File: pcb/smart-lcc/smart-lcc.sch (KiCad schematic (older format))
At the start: 12 parts, among them J1 Control board connector, J2 Aux connector, J3 Conn_01x24 (mirrored), SW1 SW_Push, SW2 SW_Push, U1 ABX00027

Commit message: WIP
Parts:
- removed J1: Control board connector, Connector_PinHeader_2.54mm:PinHeader_1x06_P2.54mm_Vertical, symbol Connector:Conn_01x06_Male
- added J1: 280372-1, TE_280372-1, symbol TE_280372-1:280372-1
- C3: footprint Capacitor_SMD:C_0603_1608Metric -> Capacitor_SMD:C_1206_3216Metric
- R1, R2: footprint Resistor_SMD:R_0402_1005Metric -> Resistor_SMD:R_0603_1608Metric
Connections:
- net +12V: now also J1.1
- net 3V3_MCU: now also J1.6
- net 3V3_OLED: now also J1.5
- net GND: now also J1.4
- net RX_FROM_CONTROL_BOARD_5V: now also J1.3
- net TX_TO_CONTROL_BOARD: now also J1.2
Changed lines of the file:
@@
 F 0 "R2" V 1243 3700 50  0000 C CNN
 F 1 "3K3" V 1334 3700 50  0000 C CNN
-F 2 "Resistor_SMD:R_0402_1005Metric" V 1380 3700 50  0001 C CNN
+F 2 "Resistor_SMD:R_0603_1608Metric" V 1380 3700 50  0001 C CNN
 F 3 "~" H 1450 3700 50  0001 C CNN
 	1    1450 3700
@@
 F 0 "R1" V 943 3700 50  0000 C CNN
 F 1 "2K2" V 1034 3700 50  0000 C CNN
-F 2 "Resistor_SMD:R_0402_1005Metric" V 1080 3700 50  0001 C CNN
+F 2 "Resistor_SMD:R_0603_1608Metric" V 1080 3700 50  0001 C CNN
 F 3 "~" H 1150 3700 50  0001 C CNN
 	1    1150 3700
 	0    1    1    0
 $EndComp
-Text GLabel 1050 1050 2    50   Output ~ 0
+Text GLabel 1750 950  0    50   Output ~ 0
 RX_FROM_CONTROL_BOARD_5V
-Text GLabel 1050 950  2    50   Input ~ 0
+Text GLabel 1750 850  0    50   Input ~ 0
 TX_TO_CONTROL_BOARD
 $Comp
@@
 Text GLabel 1050 2150 2    50   UnSpc ~ 0
 3V3_OLED
-Text GLabel 1050 1250 2    50   UnSpc ~ 0
+Text GLabel 1750 1150 0    50   UnSpc ~ 0
 3V3_OLED
 $Comp
@@
 L power:+12V #PWR0103
 U 1 1 60D7DDC1
-P 1050 850
-F 0 "#PWR0103" H 1050 700 50  0001 C CNN
-F 1 "+12V" V 1065 978 50  0000 L CNN
-F 2 "" H 1050 850 50  0001 C CNN
-F 3 "" H 1050 850 50  0001 C CNN
-	1    1050 850
-	0    1    1    0
+P 1750 750
+F 0 "#PWR0103" H 1750 600 50  0001 C CNN
+F 1 "+12V" V 1765 878 50  0000 L CNN
+F 2 "" H 1750 750 50  0001 C CNN
+F 3 "" H 1750 750 50  0001 C CNN
+	1    1750 750
+	0    -1   -1   0
 $EndComp
 $Comp
@@
 L power:GND #PWR0101
 U 1 1 60D7C577
-P 1050 1150
-F 0 "#PWR0101" H 1050 900 50  0001 C CNN
-F 1 "GND" V 1055 1022 50  0000 R CNN
-F 2 "" H 1050 1150 50  0001 C CNN
-F 3 "" H 1050 1150 50  0001 C CNN
-	1    1050 1150
-	0    -1   -1   0
+P 1750 1050
+F 0 "#PWR0101" H 1750 800 50  0001 C CNN
+F 1 "GND" V 1755 922 50  0000 R CNN
+F 2 "" H 1750 1050 50  0001 C CNN
+F 3 "" H 1750 1050 50  0001 C CNN
+	1    1750 1050
+	0    1    1    0
 $EndComp
 $Comp
@@
 Text GLabel 4350 1950 0    50   UnSpc ~ 0
 3V3_OLED
-$Comp
-L Connector:Conn_01x06_Male J1
-U 1 1 60D7884D
-P 850 1050
-F 0 "J1" H 958 1431 50  0000 C CNN
-F 1 "Control board connector" H 958 1340 50  0000 C CNN
-F 2 "Connector_PinHeader_2.54mm:PinHeader_1x06_P2.54mm_Vertical" H 850 1050 50  0001 C CNN
-F 3 "~" H 850 1050 50  0001 C CNN
-	1    850  1050
-	1    0    0    -1
-$EndComp
-Text GLabel 1050 1350 2    50   UnSpc ~ 0
+Text GLabel 1750 1250 0    50   UnSpc ~ 0
 3V3_MCU
 Text GLabel 1050 2250 2    50   UnSpc ~ 0
@@
 F 0 "C3" V 3621 4300 50  0000 C CNN
 F 1 "0.1 µF / 25V, X7R" V 3712 4300 50  0000 C CNN
-F 2 "Capacitor_SMD:C_0603_1608Metric" H 3850 4300 50  0001 C CNN
+F 2 "Capacitor_SMD:C_1206_3216Metric" H 3850 4300 50  0001 C CNN
 F 3 "~" H 3850 4300 50  0001 C CNN
 	1    3850 4300
@@
 	0    1    1    0
 $EndComp
+$Comp
+L TE_280372-1:280372-1 J1
+U 1 1 60D8FA50
+P 2150 1050
+F 0 "J1" H 2380 1146 50  0000 L CNN
+F 1 "280372-1" H 2380 1055 50  0000 L CNN
+F 2 "TE_280372-1" H 2150 1050 50  0001 L BNN
+F 3 "" H 2150 1050 50  0001 L BNN
+F 4 "Connector" H 2150 1050 50  0001 L BNN "Product_Type"
+F 5 "2.54 mm[.1 in]" H 2150 1050 50  0001 L BNN "Centerline_Pitch"
+F 6 "6" H 2150 1050 50  0001 L BNN "Number_of_Positions"
+F 7 "280372-1" H 2150 1050 50  0001 L BNN "Comment"
+F 8 "Compliant" H 2150 1050 50  0001 L BNN "EU_RoHS_Compliance"
+	1    2150 1050
+	1    0    0    -1
+$EndComp
 $EndSCHEMATC

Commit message: WIP
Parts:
- added JP1: SolderJumper_2_Open, Jumper:SolderJumper-2_P1.3mm_Open_RoundedPad1.0x1.5mm, symbol Jumper:SolderJumper_2_Open
- added JP2: SolderJumper_2_Bridged, Jumper:SolderJumper-2_P1.3mm_Bridged_RoundedPad1.0x1.5mm, symbol Jumper:SolderJumper_2_Bridged
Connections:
- net +12V: now also JP1.1 (A); no longer U1.15 (VIN)
- net +3V3: now also JP2.2 (B)
- net 3V3_MCU: now also JP2.1 (A)
- net SSD1309_DC: now also U1.20 (D2); no longer U1.10 (A6)
- net SSD1309_RES: now also U1.21 (D3/PWM); no longer U1.11 (A7)
- net SW_MINUS: now also U1.23 (D5/PWM); no longer U1.22 (D4)
- net SW_PLUS: now also U1.22 (D4); no longer U1.23 (D5/PWM)
- new net VIN: JP1.2 (B), U1.15 (VIN)
- no-connect marks 14 -> 12
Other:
- moved on the sheet: C2, C3
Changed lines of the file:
@@
 Text GLabel 8350 3000 2    50   Output ~ 0
 SSD1309_MOSI
-Text GLabel 6950 3000 0    50   Output ~ 0
+Text GLabel 8350 2100 2    50   Output ~ 0
 SSD1309_DC
-Text GLabel 6950 3100 0    50   Output ~ 0
+Text GLabel 8350 2200 2    50   Output ~ 0
 SSD1309_RES
 Text GLabel 8350 2900 2    50   Output ~ 0
@@
 L power:+12V #PWR0130
 U 1 1 60D9A09F
-P 8350 1700
-F 0 "#PWR0130" H 8350 1550 50  0001 C CNN
-F 1 "+12V" V 8365 1828 50  0000 L CNN
-F 2 "" H 8350 1700 50  0001 C CNN
-F 3 "" H 8350 1700 50  0001 C CNN
-	1    8350 1700
-	0    1    1    0
+P 3200 5450
+F 0 "#PWR0130" H 3200 5300 50  0001 C CNN
+F 1 "+12V" V 3215 5578 50  0000 L CNN
+F 2 "" H 3200 5450 50  0001 C CNN
+F 3 "" H 3200 5450 50  0001 C CNN
+	1    3200 5450
+	0    -1   -1   0
 $EndComp
 NoConn ~ 8350 1800
@@
 Text GLabel 1850 2950 3    50   Output ~ 0
 SW_PLUS
+Text GLabel 8350 2400 2    50   Input ~ 0
+SW_MINUS
 Text GLabel 8350 2300 2    50   Input ~ 0
-SW_MINUS
-Text GLabel 8350 2400 2    50   Input ~ 0
 SW_PLUS
-NoConn ~ 8350 2200
-NoConn ~ 8350 2100
 NoConn ~ 6950 2100
 NoConn ~ 6950 2200
@@
 NoConn ~ 4350 2950
 Wire Wire Line
-	3750 3950 3750 4300
-Connection ~ 3950 3950
+	3200 4150 3200 4500
+Connection ~ 3400 4150
 Wire Wire Line
-	3950 3950 3950 4300
-Connection ~ 4100 3950
-Wire Wire Line
-	4100 3950 4100 3750
-Wire Wire Line
-	4100 3950 3950 3950
+	3400 4150 3400 4500
 $Comp
 L power:+12V #PWR0125
 U 1 1 60D94DE0
-P 4100 3950
-F 0 "#PWR0125" H 4100 3800 50  0001 C CNN
-F 1 "+12V" H 4115 4123 50  0000 C CNN
-F 2 "" H 4100 3950 50  0001 C CNN
-F 3 "" H 4100 3950 50  0001 C CNN
-	1    4100 3950
+P 3750 4150
+F 0 "#PWR0125" H 3750 4000 50  0001 C CNN
+F 1 "+12V" H 3765 4323 50  0000 C CNN
+F 2 "" H 3750 4150 50  0001 C CNN
+F 3 "" H 3750 4150 50  0001 C CNN
+	1    3750 4150
 	-1   0    0    1
 $EndComp
-Connection ~ 3750 4300
+Connection ~ 3200 4500
 Wire Wire Line
-	3600 4300 3750 4300
+	3050 4500 3200 4500
 $Comp
 L power:GND #PWR0124
 U 1 1 60D925DE
-P 3600 4300
-F 0 "#PWR0124" H 3600 4050 50  0001 C CNN
-F 1 "GND" H 3605 4127 50  0000 C CNN
-F 2 "" H 3600 4300 50  0001 C CNN
-F 3 "" H 3600 4300 50  0001 C CNN
-	1    3600 4300
+P 3050 4500
+F 0 "#PWR0124" H 3050 4250 50  0001 C CNN
+F 1 "GND" H 3055 4327 50  0000 C CNN
+F 2 "" H 3050 4500 50  0001 C CNN
+F 3 "" H 3050 4500 50  0001 C CNN
+	1    3050 4500
 	1    0    0    -1
 $EndComp
@@
 L Device:C_Small C3
 U 1 1 60D9151C
-P 3850 4300
-F 0 "C3" V 3621 4300 50  0000 C CNN
-F 1 "0.1 µF / 25V, X7R" V 3712 4300 50  0000 C CNN
-F 2 "Capacitor_SMD:C_1206_3216Metric" H 3850 4300 50  0001 C CNN
-F 3 "~" H 3850 4300 50  0001 C CNN
-	1    3850 4300
+P 3300 4500
+F 0 "C3" V 3071 4500 50  0000 C CNN
+F 1 "0.1 µF / 25V, X7R" V 3162 4500 50  0000 C CNN
+F 2 "Capacitor_SMD:C_1206_3216Metric" H 3300 4500 50  0001 C CNN
+F 3 "~" H 3300 4500 50  0001 C CNN
+	1    3300 4500
 	0    1    1    0
 $EndComp
@@
 L Device:C_Small C2
 U 1 1 60D8F384
-P 3850 3950
-F 0 "C2" V 3621 3950 50  0000 C CNN
-F 1 "4.7µF / 25V, X7R" V 3712 3950 50  0000 C CNN
-F 2 "Capacitor_SMD:C_1206_3216Metric" H 3850 3950 50  0001 C CNN
-F 3 "~" H 3850 3950 50  0001 C CNN
-	1    3850 3950
+P 3300 4150
+F 0 "C2" V 3071 4150 50  0000 C CNN
+F 1 "4.7µF / 25V, X7R" V 3162 4150 50  0000 C CNN
+F 2 "Capacitor_SMD:C_1206_3216Metric" H 3300 4150 50  0001 C CNN
+F 3 "~" H 3300 4150 50  0001 C CNN
+	1    3300 4150
 	0    1    1    0
 $EndComp
@@
 	1    0    0    -1
 $EndComp
+Text GLabel 8350 1700 2    50   UnSpc ~ 0
+VIN
+$Comp
+L Jumper:SolderJumper_2_Open JP1
+U 1 1 60DA70BB
+P 3350 5450
+F 0 "JP1" H 3350 5655 50  0000 C CNN
+F 1 "SolderJumper_2_Open" H 3350 5564 50  0000 C CNN
+F 2 "Jumper:SolderJumper-2_P1.3mm_Open_RoundedPad1.0x1.5mm" H 3350 5450 50  0001 C CNN
+F 3 "~" H 3350 5450 50  0001 C CNN
+	1    3350 5450
+	1    0    0    -1
+$EndComp
+Text GLabel 3500 5450 2    50   UnSpc ~ 0
+VIN
+$Comp
+L Jumper:SolderJumper_2_Bridged JP2
+U 1 1 60DA997A
+P 3350 5900
+F 0 "JP2" H 3350 6105 50  0000 C CNN
+F 1 "SolderJumper_2_Bridged" H 3350 6014 50  0000 C CNN
+F 2 "Jumper:SolderJumper-2_P1.3mm_Bridged_RoundedPad1.0x1.5mm" H 3350 5900 50  0001 C CNN
+F 3 "~" H 3350 5900 50  0001 C CNN
+	1    3350 5900
+	1    0    0    -1
+$EndComp
+Text GLabel 3200 5900 0    50   UnSpc ~ 0
+3V3_MCU
+$Comp
+L power:+3V3 #PWR0111
+U 1 1 60DAA2F1
+P 3500 5900
+F 0 "#PWR0111" H 3500 5750 50  0001 C CNN
+F 1 "+3V3" V 3515 6028 50  0000 L CNN
+F 2 "" H 3500 5900 50  0001 C CNN
+F 3 "" H 3500 5900 50  0001 C CNN
+	1    3500 5900
+	0    1    1    0
+$EndComp
+Wire Wire Line
+	4100 3750 4100 4150
+Connection ~ 3750 4150
+Wire Wire Line
+	3400 4150 3750 4150
+Wire Wire Line
+	3750 4150 4100 4150
 $EndSCHEMATC

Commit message: Getting ready to manufacture PCB
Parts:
- R1, R2, R3: footprint Resistor_SMD:R_0603_1608Metric -> Resistor_SMD:R_1206_3216Metric
- SW1, SW2: footprint Button_Switch_SMD:SW_Push_1P1T_NO_6x6mm_H9.5mm -> SW_Push_ADTSMW65:ADTSMW65
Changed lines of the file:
@@
 F 0 "R2" V 1243 3700 50  0000 C CNN
 F 1 "3K3" V 1334 3700 50  0000 C CNN
-F 2 "Resistor_SMD:R_0603_1608Metric" V 1380 3700 50  0001 C CNN
+F 2 "Resistor_SMD:R_1206_3216Metric" V 1380 3700 50  0001 C CNN
 F 3 "~" H 1450 3700 50  0001 C CNN
 	1    1450 3700
@@
 F 0 "R1" V 943 3700 50  0000 C CNN
 F 1 "2K2" V 1034 3700 50  0000 C CNN
-F 2 "Resistor_SMD:R_0603_1608Metric" V 1080 3700 50  0001 C CNN
+F 2 "Resistor_SMD:R_1206_3216Metric" V 1080 3700 50  0001 C CNN
 F 3 "~" H 1150 3700 50  0001 C CNN
 	1    1150 3700
@@
 F 0 "SW2" H 1650 3235 50  0000 C CNN
 F 1 "SW_Push" H 1650 3144 50  0000 C CNN
-F 2 "Button_Switch_SMD:SW_Push_1P1T_NO_6x6mm_H9.5mm" H 1650 3150 50  0001 C CNN
+F 2 "SW_Push_ADTSMW65:ADTSMW65" H 1650 3150 50  0001 C CNN
 F 3 "~" H 1650 3150 50  0001 C CNN
 	1    1650 2950
@@
 F 0 "SW1" H 950 3235 50  0000 C CNN
 F 1 "SW_Push" H 950 3144 50  0000 C CNN
-F 2 "Button_Switch_SMD:SW_Push_1P1T_NO_6x6mm_H9.5mm" H 950 3150 50  0001 C CNN
+F 2 "SW_Push_ADTSMW65:ADTSMW65" H 950 3150 50  0001 C CNN
 F 3 "~" H 950 3150 50  0001 C CNN
 	1    950  2950
@@
 F 0 "R3" V 4157 3550 50  0000 C CNN
 F 1 "910K" V 4066 3550 50  0000 C CNN
-F 2 "Resistor_SMD:R_0603_1608Metric" V 3880 3550 50  0001 C CNN
+F 2 "Resistor_SMD:R_1206_3216Metric" V 3880 3550 50  0001 C CNN
 F 3 "~" H 3950 3550 50  0001 C CNN
 	1    3950 3550

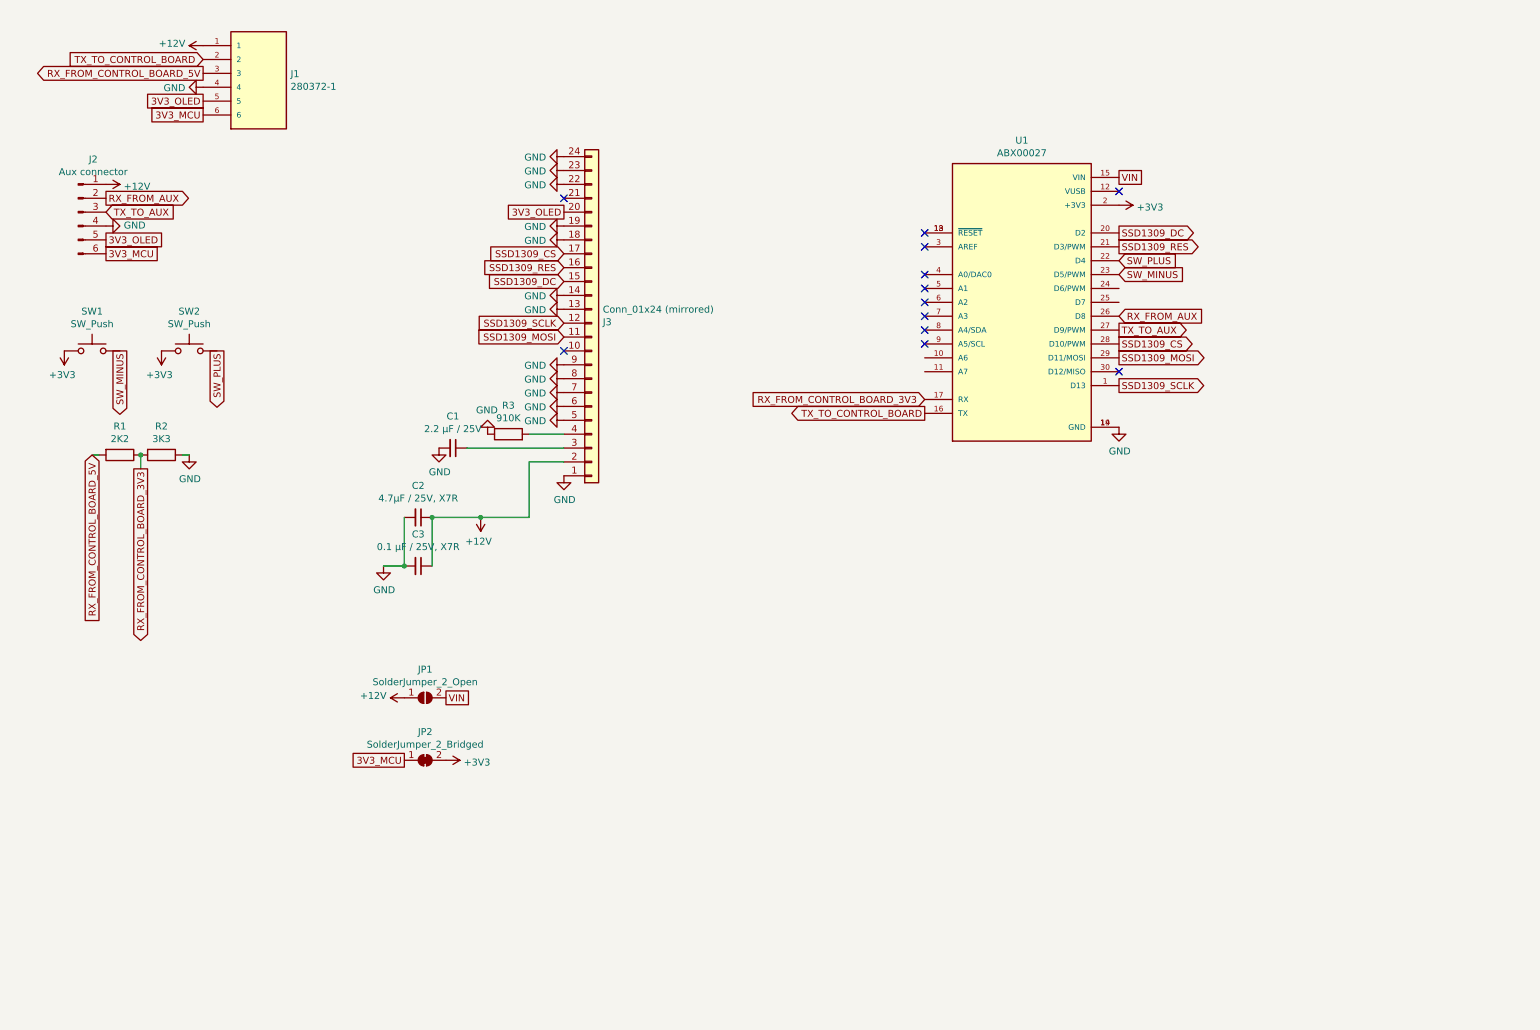
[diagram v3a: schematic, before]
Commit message: Started work on a rev b board
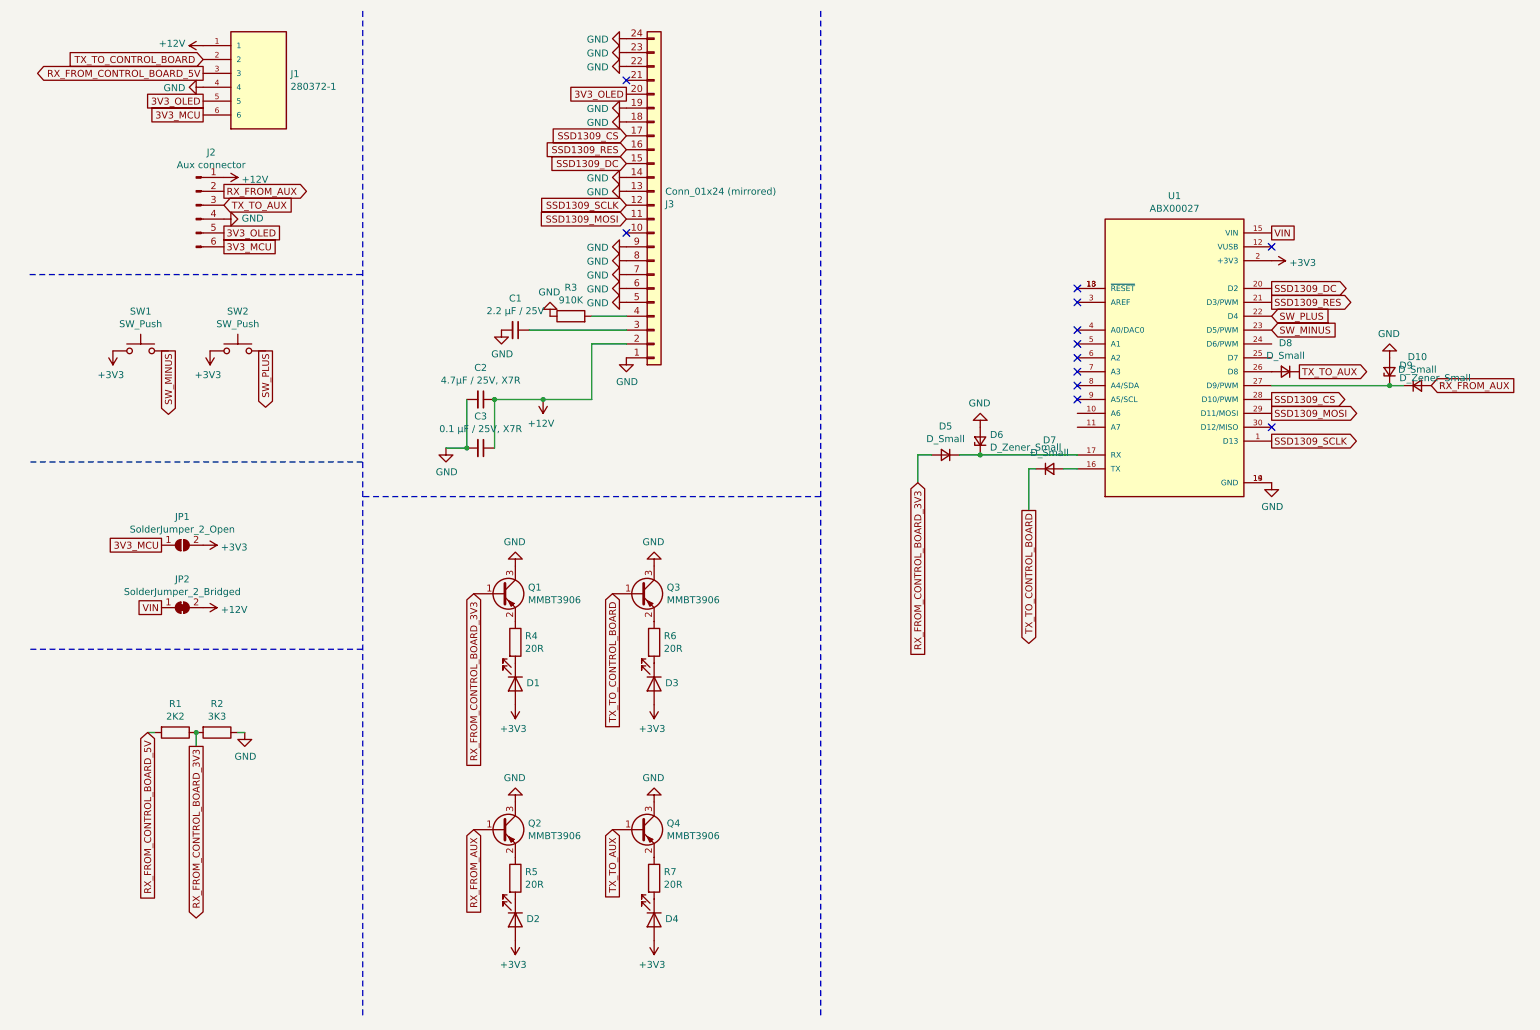
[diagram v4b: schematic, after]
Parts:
- added D1, D2, D3, D4: 19-217/BHC-ZL1M2RY/3T, LED_SMD:LED_0603_1608Metric, symbol Device:LED
- added D10, D5, D7, D8: D_Small, Diode_SMD:D_SOD-123F, symbol Device:D_Small
- added D6, D9: D_Zener_Small, Diode_SMD:D_SOD-123, symbol Device:D_Zener_Small
- added Q1, Q2, Q3, Q4: MMBT3906, Package_TO_SOT_SMD:SOT-23, symbol Transistor_BJT:MMBT3906
- added R4, R5, R6, R7: 20R, Resistor_SMD:R_0603_1608Metric, symbol Device:R
- C1: footprint Capacitor_SMD:C_1206_3216Metric -> Capacitor_SMD:C_0603_1608Metric
- C2, C3: footprint Capacitor_SMD:C_1206_3216Metric -> Capacitor_SMD:C_0402_1005Metric
- R1, R2: footprint Resistor_SMD:R_1206_3216Metric -> Resistor_SMD:R_0402_1005Metric
- R3: footprint Resistor_SMD:R_1206_3216Metric -> Resistor_SMD:R_0603_1608Metric
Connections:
- net +12V: now also JP2.2 (B); no longer JP1.1 (A)
- net +3V3: now also JP1.2 (B), D1.2 (A), D2.2 (A), D3.2 (A), D4.2 (A); no longer JP2.2 (B)
- net 3V3_MCU: now also JP1.1 (A); no longer JP2.1 (A)
- net GND: now also D6.2 (A), D9.2 (A), Q1.3 (C), Q2.3 (C), Q3.3 (C), Q4.3 (C)
- net RX_FROM_AUX: now also D10.2 (A), Q2.1 (B); no longer U1.26 (D8)
- net RX_FROM_CONTROL_BOARD_3V3: now also D5.2 (A), Q1.1 (B); no longer U1.17 (RX)
- net TX_TO_AUX: now also D8.1 (K), Q4.1 (B); no longer U1.27 (D9/PWM)
- net TX_TO_CONTROL_BOARD: now also D7.1 (K), Q3.1 (B); no longer U1.16 (TX)
- net VIN: now also JP2.1 (A); no longer JP1.2 (B)
- new net: D7.2 (A), U1.16 (TX)
- new net: D5.1 (K), D6.1 (K), U1.17 (RX)
- new net: D8.2 (A), U1.26 (D8)
- new net: D10.1 (K), D9.1 (K), U1.27 (D9/PWM)
- new net: Q1.2 (E), R4.1
- new net: D1.1 (K), R4.2
- new net: Q3.2 (E), R6.1
- new net: D3.1 (K), R6.2
- new net: Q2.2 (E), R5.1
- new net: D2.1 (K), R5.2
- new net: Q4.2 (E), R7.1
- new net: D4.1 (K), R7.2
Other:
- moved on the sheet: C1, C2, C3, J2, J3, JP1, JP2, R1, R2, R3, SW1, SW2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

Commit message: WIP
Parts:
- removed Q1, Q2, Q3, Q4: MMBT3906, Package_TO_SOT_SMD:SOT-23, symbol Transistor_BJT:MMBT3906
- added U2, U3: LPV358, Package_SO:VSSOP-8_3.0x3.0mm_P0.65mm, symbol Amplifier_Operational:LM358
- C1: Comment (none) -> Per display data sheet reference design; JLCPCB Basic (none) -> N; LCSC (none) -> C57895
- C2: footprint Capacitor_SMD:C_0402_1005Metric -> Capacitor_SMD:C_0805_2012Metric; Comment (none) -> Per display data sheet reference design; JLCPCB Basic (none) -> N; LCSC (none) -> C98195
- C3: footprint Capacitor_SMD:C_0402_1005Metric -> Capacitor_SMD:C_0603_1608Metric; Comment (none) -> Per display data sheet reference design, part is 50V; JLCPCB Basic (none) -> Y; LCSC (none) -> C14663
- D1, D2, D3, D4: JLCPCB Basic (none) -> Y; LCSC (none) -> C72041
- D10, D5, D7, D8: footprint Diode_SMD:D_SOD-123F -> Diode_SMD:D_SOD-123; JLCPCB Basic (none) -> Y; LCSC (none) -> C8598
- D6, D9: JLCPCB Basic (none) -> N; LCSC (none) -> C707129
- J1: Comment 280372-1 -> (none)
- J3: JLCPCB Basic (none) -> N; LCSC (none) -> C506794
- R1: JLCPCB Basic (none) -> N; LCSC (none) -> C138019
- R2: JLCPCB Basic (none) -> N; LCSC (none) -> C137993
- R3: JLCPCB Basic (none) -> N; LCSC (none) -> C141274
- R4, R5, R6, R7: JLCPCB Basic (none) -> Y; LCSC (none) -> C22950
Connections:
- net +3V3: now also U2.8 (V+), U3.8 (V+); no longer D1.2 (A), D2.2 (A), D3.2 (A), D4.2 (A)
- net GND: now also D1.1 (K), D2.1 (K), D3.1 (K), D4.1 (K), U2.4 (V-), U3.4 (V-)
- net RX_FROM_AUX: now also U3.2 (-)
- net RX_FROM_CONTROL_BOARD_3V3: now also U2.2 (-)
- net TX_TO_AUX: now also U3.6 (-)
- net TX_TO_CONTROL_BOARD: now also U2.6 (-)
- net at R4.1: now also D1.2 (A)
- net at R4.2: now also U2.1, U2.3 (+); no longer D1.1 (K)
- net at R6.1: now also D3.2 (A)
- net at R6.2: now also U2.5 (+), U2.7; no longer D3.1 (K)
- net at R5.1: now also D2.2 (A)
- net at R5.2: now also U3.5 (+), U3.7; no longer D2.1 (K)
- net at R7.1: now also D4.2 (A)
- net at R7.2: now also U3.1, U3.3 (+); no longer D4.1 (K)
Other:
- moved on the sheet: D1, D2, D3, D4, R4, R5, R6, R7
